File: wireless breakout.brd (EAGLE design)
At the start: 45.7 x 45.7 mm, 5 parts

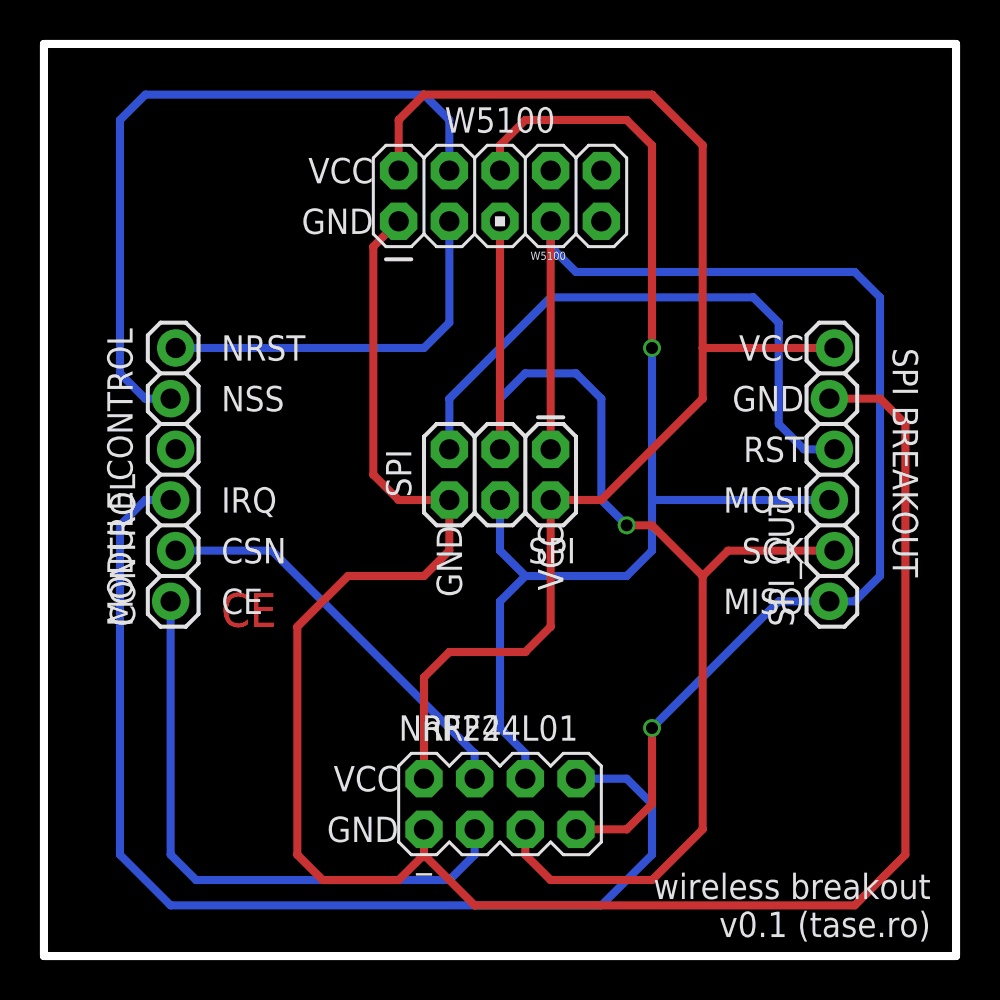
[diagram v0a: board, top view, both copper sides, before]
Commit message: Flipped the nrf24 connector around.
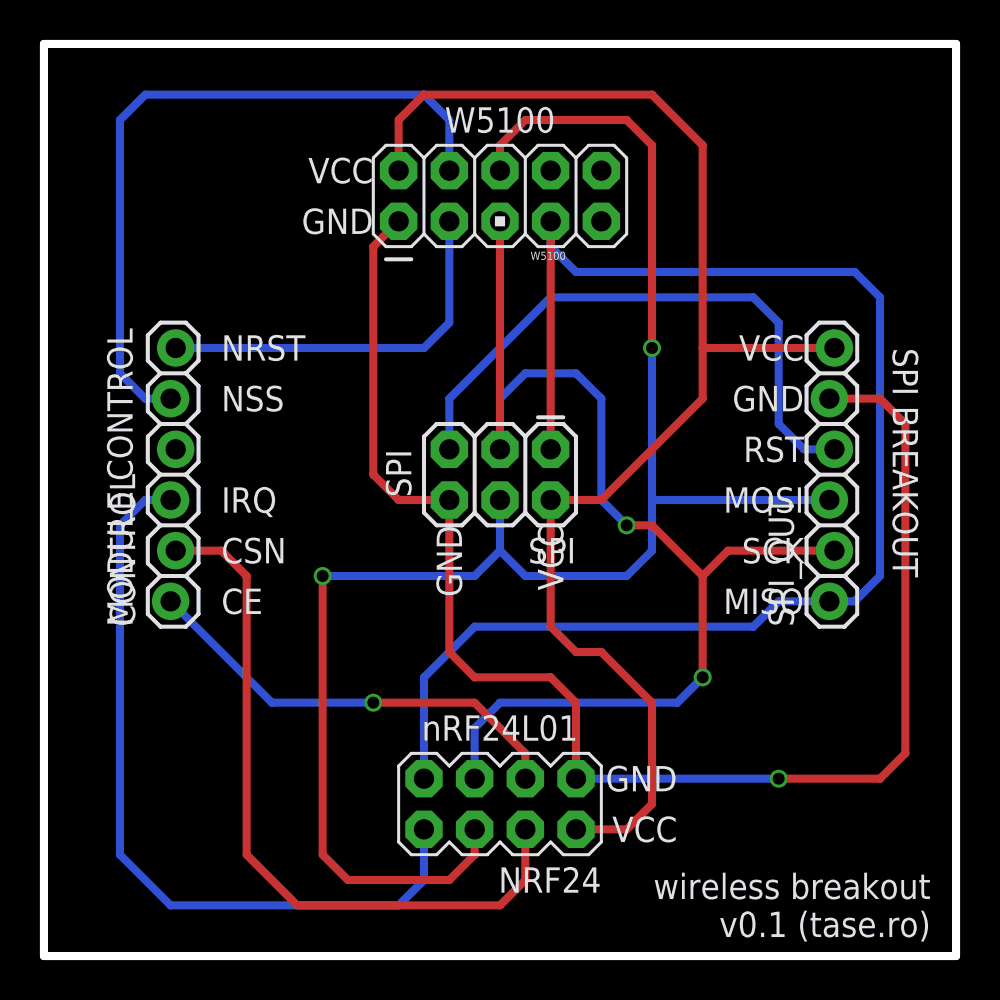
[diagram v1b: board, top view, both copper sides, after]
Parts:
- turned NRF24 to 180 degrees
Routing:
- net GND: track 101.6 -> 74.3 mm, vias 0 -> 1
- net MOSI: track 61.6 -> 83.7 mm, vias 1 -> 2
- net IRQ: track 55.2 -> 38.9 mm
- net CSN: track 20.5 -> 36.1 mm
- net CE: track 30.3 -> 22.2 mm, vias 0 -> 1
- net MISO: track 67.0 -> 74.3 mm, vias 1 -> 0
- net SCK: track 63.4 -> 59.1 mm, vias 1 -> 2
- net VCC: track 67.2 -> 70.8 mm
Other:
- board text removed: "_"
